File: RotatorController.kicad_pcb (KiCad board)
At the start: 2 copper layers, 100 x 70.9 mm, 59 parts, among them J1 USB_A, J2 26 VAC, J3 Rotator, J4 Motor Cap, K1 G5LE-1, K2 G5LE-1, K3 G5LE-1, Q1 BSS123, Q2 BSS123, Q3 BSS123, SW1 SW_CW, SW2 SW_CCW, U1 Teensy4.0, U3 AP2161W

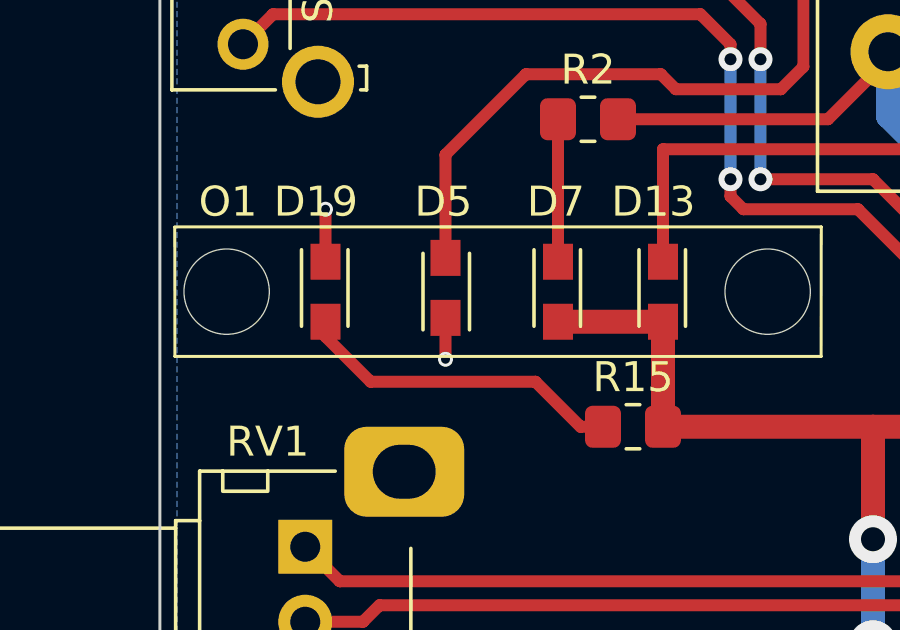
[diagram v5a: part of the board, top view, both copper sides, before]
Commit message: Added OSHPark pcb design rules fixed a few design rule checks
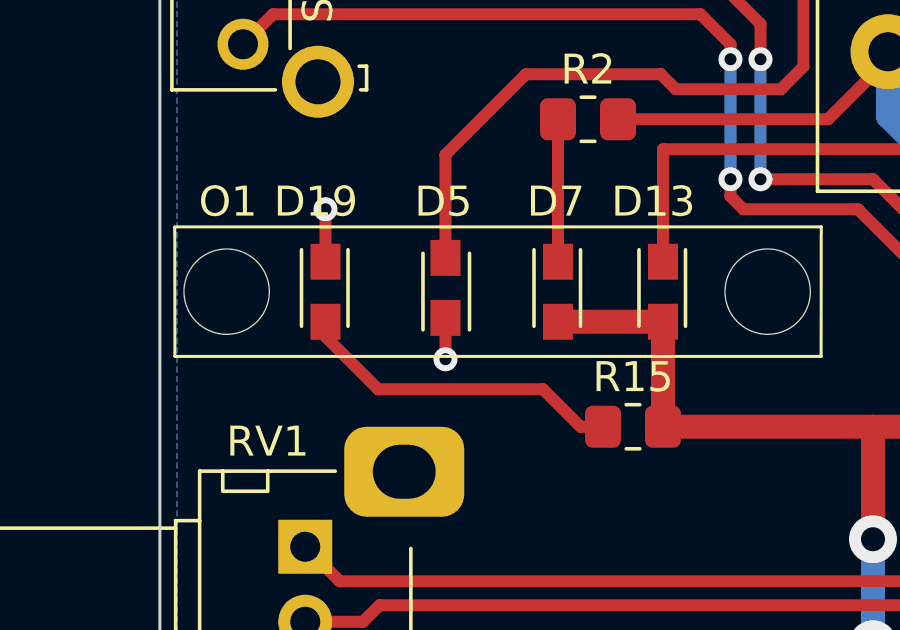
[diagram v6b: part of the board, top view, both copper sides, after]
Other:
- rule pad_to_mask_clearance: 0 -> 0.0508
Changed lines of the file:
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@@
   )
   (setup
-    (pad_to_mask_clearance 0)
+    (stackup
+      (layer "F.SilkS" (type "Top Silk Screen"))
+      (layer "F.Paste" (type "Top Solder Paste"))
+      (layer "F.Mask" (type "Top Solder Mask") (thickness 0.01))
+      (layer "F.Cu" (type "copper") (thickness 0.035))
+      (layer "dielectric 1" (type "core") (thickness 1.51) (material "FR4") (epsilon_r 4.5) (loss_tangent 0.02))
+      (layer "B.Cu" (type "copper") (thickness 0.035))
+      (layer "B.Mask" (type "Bottom Solder Mask") (thickness 0.01))
+      (layer "B.Paste" (type "Bottom Solder Paste"))
+      (layer "B.SilkS" (type "Bottom Silk Screen"))
+      (copper_finish "None")
+      (dielectric_constraints no)
+    )
+    (pad_to_mask_clearance 0.0508)
     (grid_origin 195.2 79.4)
     (pcbplotparams
@@
         (effects (font (size 1 1) (thickness 0.15)))
     )
-    (fp_text value "26VAC" (at 0 -1.75 90) (layer "F.Fab")
+    (fp_text value "26VAC" (at 0 1.679408 90) (layer "F.Fab")
         (effects (font (size 1 1) (thickness 0.15)))
     )
@@
         (effects (font (size 1 1) (thickness 0.15)))
     )
-    (fp_text value "5V" (at 0 -1.75 -90) (layer "F.Fab")
+    (fp_text value "5V" (at 0 -1.929408 -90) (layer "F.Fab")
         (effects (font (size 1 1) (thickness 0.15)))
     )
@@
   (segment (start 160.145592 74.275) (end 164.200592 70.22) (width 0.8) (layer "B.Cu") (net 1))
   (segment (start 172.380592 70.22) (end 172.380592 75.9275) (width 0.8) (layer "B.Cu") (net 1))
-  (segment (start 99.520592 91.4) (end 94.025464 91.4) (width 0.4) (layer "F.Cu") (net 2))
-  (segment (start 101.770592 92.9) (end 101.020592 92.9) (width 0.4) (layer "F.Cu") (net 2))
+  (segment (start 99.770592 91.65) (end 94.275464 91.65) (width 0.4) (layer "F.Cu") (net 2))
+  (segment (start 94.275464 91.65) (end 92.520592 89.895128) (width 0.4) (layer "F.Cu") (net 2))
   (segment (start 92.520592 89.895128) (end 92.520592 89.275) (width 0.4) (layer "F.Cu") (net 2))
-  (segment (start 101.020592 92.9) (end 99.520592 91.4) (width 0.4) (layer "F.Cu") (net 2))
-  (segment (start 94.025464 91.4) (end 92.520592 89.895128) (width 0.4) (layer "F.Cu") (net 2))
+  (segment (start 101.770592 92.9) (end 101.020592 92.9) (width 0.4) (layer "F.Cu") (net 2))
+  (segment (start 101.020592 92.9) (end 99.770592 91.65) (width 0.4) (layer "F.Cu") (net 2))
   (segment (start 131.020592 109.525) (end 134.333092 109.525) (width 0.25) (layer "F.Cu") (net 3))
   (segment (start 131.020592 114.15) (end 134.145592 114.15) (width 0.25) (layer "F.Cu") (net 3))
@@
   (via (at 108.770592 124.08) (size 0.8) (drill 0.4) (layers "F.Cu" "B.Cu") (free) (net 4))
   (via (at 139.208092 109.525) (size 0.8) (drill 0.4) (layers "F.Cu" "B.Cu") (free) (net 4))
-  (via (at 92.520592 85.65) (size 0.5) (drill 0.3) (layers "F.Cu" "B.Cu") (free) (net 4))
+  (via (at 92.520592 85.65) (size 0.8) (drill 0.4) (layers "F.Cu" "B.Cu") (free) (net 4))
   (via (at 157.2 96.65) (size 0.8) (drill 0.4) (layers "F.Cu" "B.Cu") (free) (net 4))
   (via (at 123.770592 114.65) (size 0.8) (drill 0.4) (layers "F.Cu" "B.Cu") (free) (net 4))
   (via (at 154.770592 90.0875) (size 0.8) (drill 0.4) (layers "F.Cu" "B.Cu") (free) (net 4))
-  (via (at 96.520592 90.65) (size 0.5) (drill 0.3) (layers "F.Cu" "B.Cu") (free) (net 4))
+  (via (at 96.520592 90.65) (size 0.8) (drill 0.4) (layers "F.Cu" "B.Cu") (free) (net 4))
   (via (at 139.270592 114.4) (size 0.8) (drill 0.4) (layers "F.Cu" "B.Cu") (free) (net 4))
   (via (at 124.020592 109.4) (size 0.8) (drill 0.4) (layers "F.Cu" "B.Cu") (free) (net 4))

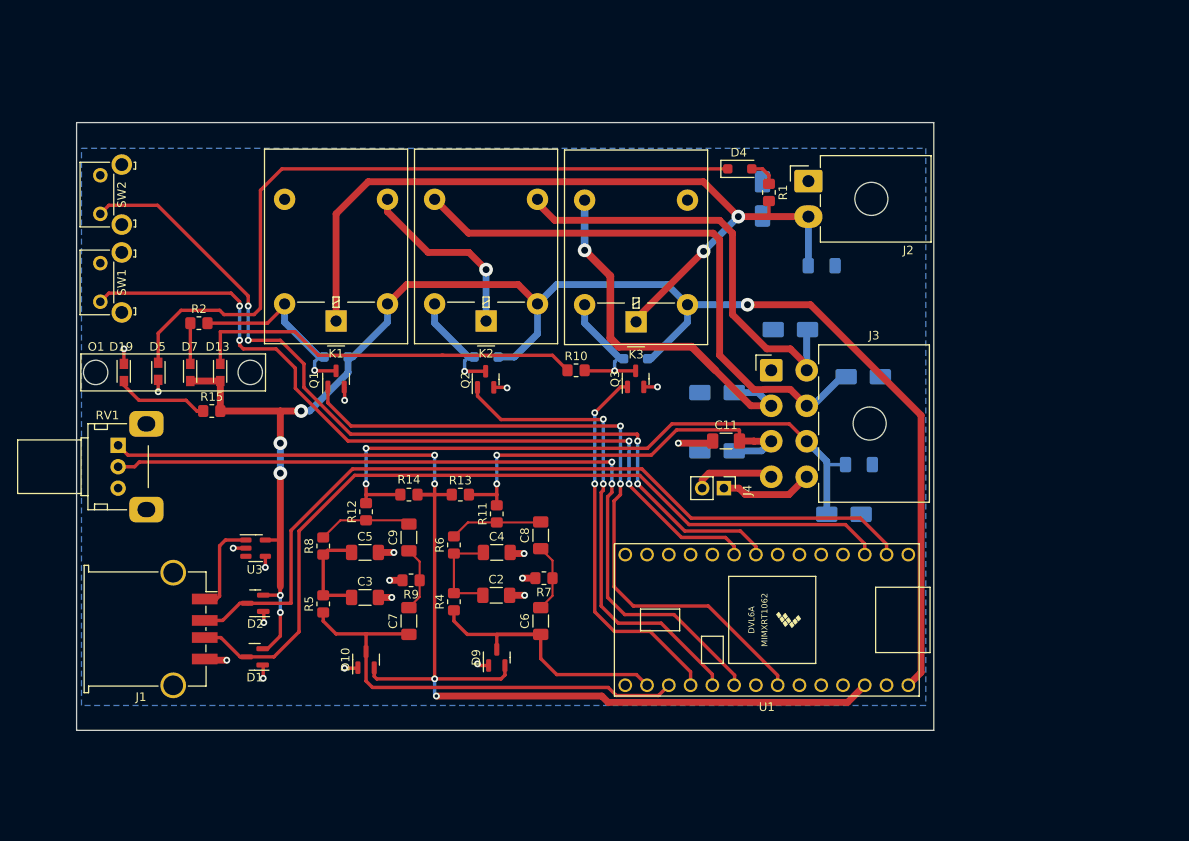
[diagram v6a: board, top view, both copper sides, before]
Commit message: Moved relays and lightpipe to make room for motor cap mounted over PCB
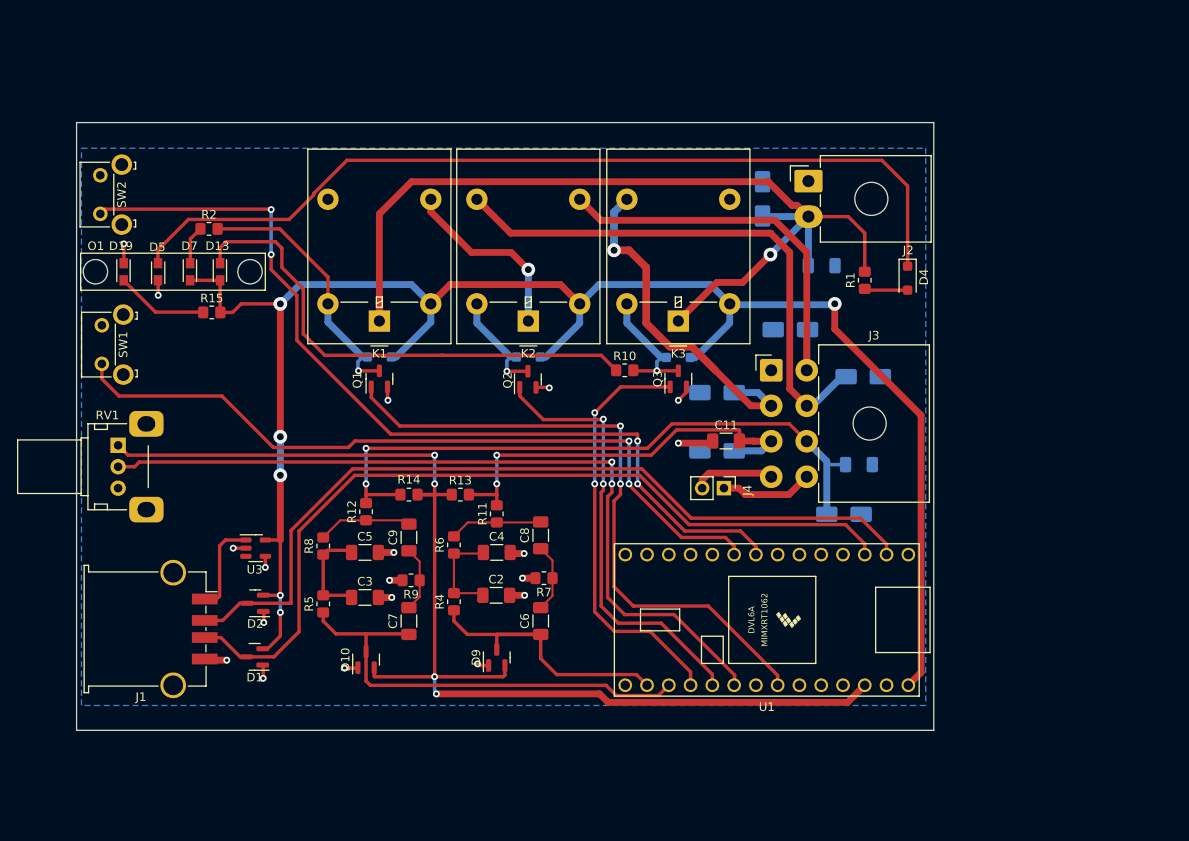
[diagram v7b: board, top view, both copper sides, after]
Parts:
- moved D4 23.4 mm to (183.9, 77.4), turned to -90 degrees
- moved R1 15.2 mm to (178.9, 77.7), turned to 90 degrees
- moved D13 11.7 mm to (103.7, 76.7)
- moved D19 11.7 mm to (92.5, 76.7)
- moved D7 11.7 mm to (100.2, 76.7)
- moved O1 11.7 mm to (89.2, 76.7)
- moved D5 11.6 mm to (96.5, 76.7)
- moved R15 11.5 mm to (102.8, 81.4)
- moved R2 11.1 mm to (102.5, 71.7)
- moved SW1 7.25 mm to (90.0, 87.4)
- moved R10 5.68 mm to (150.9, 88.2)
- moved D6 5.05 mm to (122.3, 86.6)
- moved K1 5.05 mm to (122.3, 82.4)
- moved Q1 5.05 mm to (122.3, 89.2)
- moved D12 4.98 mm to (157.2, 86.7)
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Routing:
- net Net-(D4-K): track 86.4 -> 104.0 mm
- net /+5V: track 189.4 -> 204.9 mm
- net Net-(D13-K): track 46.4 -> 59.1 mm
- net /26VAC: track 101.1 -> 109.1 mm, vias 2 -> 1
- net Net-(D6-A): track 22.8 -> 30.4 mm
- net /CW: track 94.9 -> 88.2 mm, vias 4 -> 2
- net /Mot_Ctl: track 81.0 -> 75.3 mm
- net /Brk_Ctl: track 43.9 -> 48.9 mm
- net /Dir_Ctl: track 56.3 -> 51.4 mm
- net /Right: track 67.3 -> 63.8 mm
- net /Brake: track 44.5 -> 41.2 mm
- net /Left: track 50.2 -> 47.6 mm
- net /CCW: track 102.3 -> 104.5 mm
- net Net-(D4-A): track 3.31 -> 5.06 mm
- net GND: track 33.2 -> 34.1 mm
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
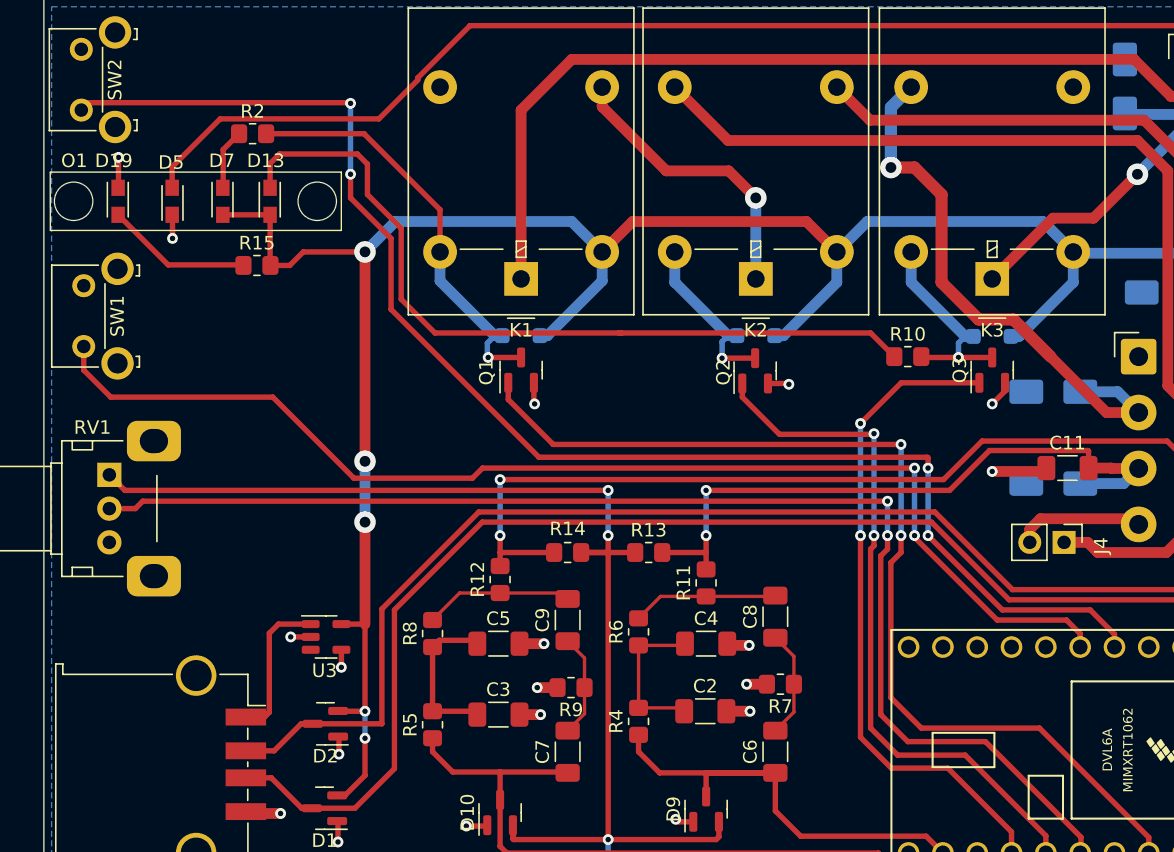
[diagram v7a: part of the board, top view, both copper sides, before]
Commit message: Board dimensions in inches tweaked layout
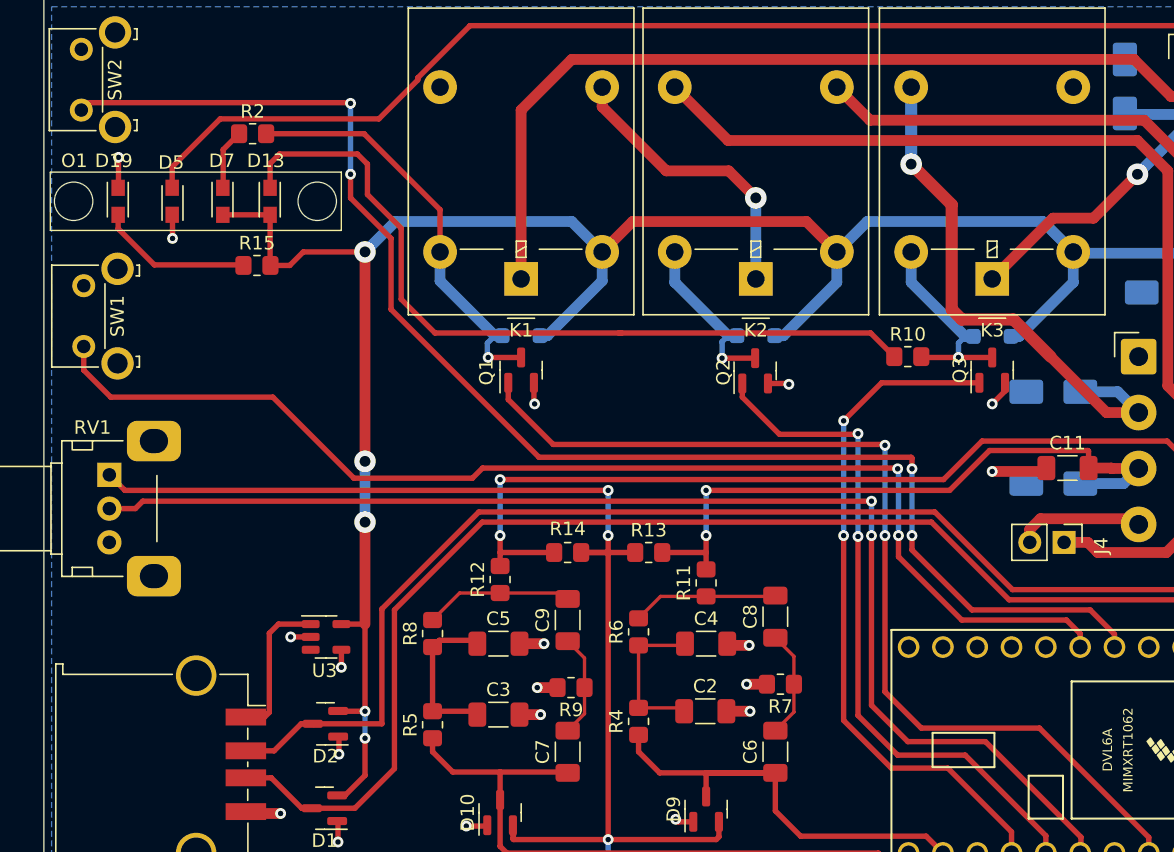
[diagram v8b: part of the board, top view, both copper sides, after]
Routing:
- net /Brk_Ctl: track 48.9 -> 50.8 mm
- net /Brake: track 41.2 -> 39.7 mm
- net /Mot_Ctl: track 75.3 -> 73.9 mm
- net /Hdg: track 93.6 -> 92.5 mm
- net /Dir_Ctl: track 51.4 -> 50.5 mm
- net /CW: track 88.2 -> 89.0 mm
- net /CCW: track 104.5 -> 105.1 mm
- net Net-(D19-A): track 10.8 -> 11.4 mm
